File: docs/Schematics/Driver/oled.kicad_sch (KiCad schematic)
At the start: 0 parts

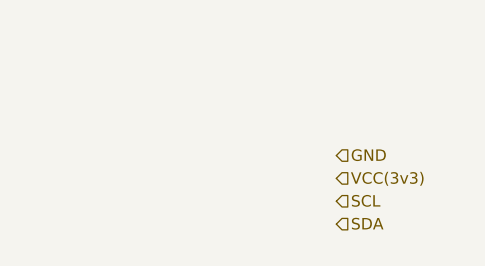
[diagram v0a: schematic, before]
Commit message: First scematic design for the card
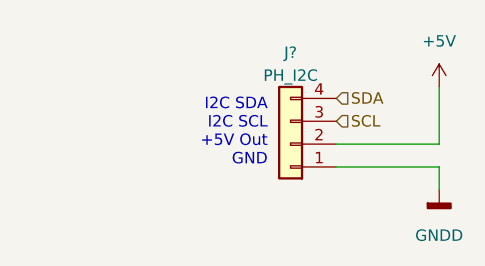
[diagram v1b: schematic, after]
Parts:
- added J?: PH_I2C, symbol Connector_Generic:Conn_01x04
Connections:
- net SCL: now also J?.3 (Pin_3)
- net SDA: now also J?.4 (Pin_4)
- new net +5V: J?.2 (Pin_2)
- new net GNDD: J?.1 (Pin_1)
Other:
- note added: "I2C SDA I2C SCL +5V Out GND"
- company: (none) -> HiQ
- title: (none) -> Arty Z7 IO expander card
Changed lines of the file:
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@@
 (kicad_sch (version 20211123) (generator eeschema)
   (paper "A4")
-  (hierarchical_label "SCL" (shape input) (at 172.72 80.01 0)
+  (title_block
+    (title "Arty Z7 IO expander card")
+    (date "2022-12-24")
+    (rev "0.1")
+    (company "HiQ")
+  )
+  (wire (pts (xy 172.72 73.66) (xy 184.15 73.66))
+    (stroke (width 0) (type default) (color 0 0 0 0))
+  )
+  (wire (pts (xy 172.72 76.2) (xy 184.15 76.2))
+    (stroke (width 0) (type default) (color 0 0 0 0))
+  )
+  (wire (pts (xy 184.15 76.2) (xy 184.15 78.74))
+    (stroke (width 0) (type default) (color 0 0 0 0))
+  )
+  (wire (pts (xy 184.15 73.66) (xy 184.15 67.31))
+    (stroke (width 0) (type default) (color 0 0 0 0))
+  )
+  (text "I2C SDA\nI2C SCL\n+5V Out\nGND" (at 165.1 76.2 180)
+    (effects (font (size 1.27 1.27)) (justify right bottom))
+  )
+  (hierarchical_label "SCL" (shape input) (at 172.72 71.12 0)
     (effects (font (size 1.27 1.27)) (justify left))
   )
-  (hierarchical_label "VCC(3v3)" (shape input) (at 172.72 77.47 0)
+  (hierarchical_label "SDA" (shape input) (at 172.72 68.58 0)
     (effects (font (size 1.27 1.27)) (justify left))
   )
-  (hierarchical_label "GND" (shape input) (at 172.72 74.93 0)
-    (effects (font (size 1.27 1.27)) (justify left))
+  (symbol (lib_id "power:GNDD") (at 184.15 78.74 0) (unit 1)
+    (in_bom yes) (on_board yes) (fields_autoplaced)
+    (property "Reference" "#PWR?" (id 0) (at 184.15 85.09 0)
+      (effects (font (size 1.27 1.27)) hide)
+    )
+    (property "Value" "GNDD" (id 1) (at 184.15 83.82 0))
+    (property "Footprint" "" (id 2) (at 184.15 78.74 0)
+      (effects (font (size 1.27 1.27)) hide)
+    )
+    (property "Datasheet" "" (id 3) (at 184.15 78.74 0)
+      (effects (font (size 1.27 1.27)) hide)
+    )
+    (pin "1")
   )
-  (hierarchical_label "SDA" (shape input) (at 172.72 82.55 0)
-    (effects (font (size 1.27 1.27)) (justify left))
+  (symbol (lib_id "power:+5V") (at 184.15 67.31 0) (unit 1)
+    (in_bom yes) (on_board yes) (fields_autoplaced)
+    (property "Reference" "#PWR?" (id 0) (at 184.15 71.12 0)
+      (effects (font (size 1.27 1.27)) hide)
+    )
+    (property "Value" "+5V" (id 1) (at 184.15 62.23 0))
+    (property "Footprint" "" (id 2) (at 184.15 67.31 0)
+      (effects (font (size 1.27 1.27)) hide)
+    )
+    (property "Datasheet" "" (id 3) (at 184.15 67.31 0)
+      (effects (font (size 1.27 1.27)) hide)
+    )
+    (pin "1")
+  )
+  (symbol (lib_id "Connector_Generic:Conn_01x04") (at 167.64 73.66 180) (unit 1)
+    (in_bom yes) (on_board yes)
+    (property "Reference" "J?" (id 0) (at 167.64 63.5 0))
+    (property "Value" "PH_I2C" (id 1) (at 167.64 66.04 0))
+    (property "Footprint" "" (id 2) (at 167.64 73.66 0)
+      (effects (font (size 1.27 1.27)) hide)
+    )
+    (property "Datasheet" "~" (id 3) (at 167.64 73.66 0)
+      (effects (font (size 1.27 1.27)) hide)
+    )
+    (pin "1")
+    (pin "2")
+    (pin "3")
+    (pin "4")
   )
 )

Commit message: Added footprints and a symbol for the level shifters
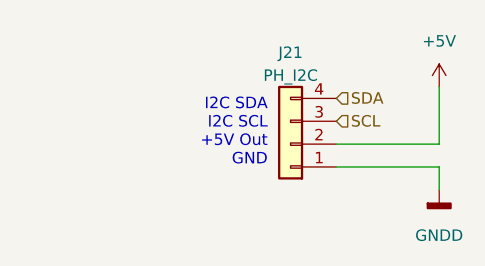
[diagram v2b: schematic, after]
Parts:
- J21: renamed from J?; footprint (none) -> Connector_PinHeader_2.54mm:PinHeader_1x04_P2.54mm_Vertical
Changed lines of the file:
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@@
   (symbol (lib_id "power:GNDD") (at 184.15 78.74 0) (unit 1)
     (in_bom yes) (on_board yes) (fields_autoplaced)
-    (property "Reference" "#PWR?" (id 0) (at 184.15 85.09 0)
+    (property "Reference" "#PWR051" (id 0) (at 184.15 85.09 0)
       (effects (font (size 1.27 1.27)) hide)
     )
@@
   (symbol (lib_id "power:+5V") (at 184.15 67.31 0) (unit 1)
     (in_bom yes) (on_board yes) (fields_autoplaced)
-    (property "Reference" "#PWR?" (id 0) (at 184.15 71.12 0)
+    (property "Reference" "#PWR050" (id 0) (at 184.15 71.12 0)
       (effects (font (size 1.27 1.27)) hide)
     )
@@
   (symbol (lib_id "Connector_Generic:Conn_01x04") (at 167.64 73.66 180) (unit 1)
     (in_bom yes) (on_board yes)
-    (property "Reference" "J?" (id 0) (at 167.64 63.5 0))
+    (property "Reference" "J21" (id 0) (at 167.64 63.5 0))
     (property "Value" "PH_I2C" (id 1) (at 167.64 66.04 0))
-    (property "Footprint" "" (id 2) (at 167.64 73.66 0)
+    (property "Footprint" "Connector_PinHeader_2.54mm:PinHeader_1x04_P2.54mm_Vertical" (id 2) (at 167.64 73.66 0)
       (effects (font (size 1.27 1.27)) hide)
     )

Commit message: Added caps and changed the connection from the motor sensors to plints
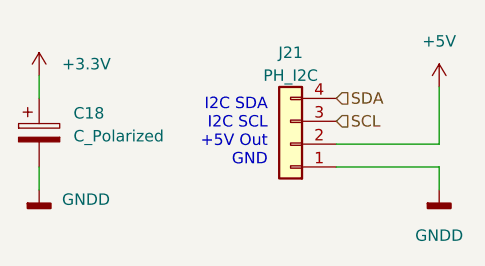
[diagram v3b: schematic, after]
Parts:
- added C18: C_Polarized, Capacitor_THT:CP_Radial_D8.0mm_P3.80mm, symbol Device:C_Polarized
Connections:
- net GNDD: now also C18.2
- new net +3.3V: C18.1
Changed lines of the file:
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@@
+    (stroke (width 0) (type default) (color 0 0 0 0))
+  )
+  (wire (pts (xy 139.7 66.04) (xy 139.7 68.58))
     (stroke (width 0) (type default) (color 0 0 0 0))
   )
   (wire (pts (xy 184.15 76.2) (xy 184.15 78.74))
+    (stroke (width 0) (type default) (color 0 0 0 0))
+  )
+  (wire (pts (xy 139.7 76.2) (xy 139.7 78.74))
     (stroke (width 0) (type default) (color 0 0 0 0))
   )
@@
   (hierarchical_label "SDA" (shape input) (at 172.72 68.58 0)
     (effects (font (size 1.27 1.27)) (justify left))
+  )
+  (symbol (lib_id "power:GNDD") (at 139.7 78.74 0) (unit 1)
+    (in_bom yes) (on_board yes) (fields_autoplaced)
+    (property "Reference" "#PWR096" (id 0) (at 139.7 85.09 0)
+      (effects (font (size 1.27 1.27)) hide)
+    )
+    (property "Value" "GNDD" (id 1) (at 142.24 79.8194 0)
+      (effects (font (size 1.27 1.27)) (justify left))
+    )
+    (property "Footprint" "" (id 2) (at 139.7 78.74 0)
+      (effects (font (size 1.27 1.27)) hide)
+    )
+    (property "Datasheet" "" (id 3) (at 139.7 78.74 0)
+      (effects (font (size 1.27 1.27)) hide)
+    )
+    (pin "1")
+  )
+  (symbol (lib_id "power:+3.3V") (at 139.7 66.04 0) (unit 1)
+    (in_bom yes) (on_board yes) (fields_autoplaced)
+    (property "Reference" "#PWR095" (id 0) (at 139.7 69.85 0)
+      (effects (font (size 1.27 1.27)) hide)
+    )
+    (property "Value" "+3.3V" (id 1) (at 142.24 64.7699 0)
+      (effects (font (size 1.27 1.27)) (justify left))
+    )
+    (property "Footprint" "" (id 2) (at 139.7 66.04 0)
+      (effects (font (size 1.27 1.27)) hide)
+    )
+    (property "Datasheet" "" (id 3) (at 139.7 66.04 0)
+      (effects (font (size 1.27 1.27)) hide)
+    )
+    (pin "1")
   )
   (symbol (lib_id "power:GNDD") (at 184.15 78.74 0) (unit 1)
@@
     (pin "1")
   )
+  (symbol (lib_id "Device:C_Polarized") (at 139.7 72.39 0) (unit 1)
+    (in_bom yes) (on_board yes) (fields_autoplaced)
+    (property "Reference" "C18" (id 0) (at 143.51 70.2309 0)
+      (effects (font (size 1.27 1.27)) (justify left))
+    )
+    (property "Value" "C_Polarized" (id 1) (at 143.51 72.7709 0)
+      (effects (font (size 1.27 1.27)) (justify left))
+    )
+    (property "Footprint" "Capacitor_THT:CP_Radial_D8.0mm_P3.80mm" (id 2) (at 140.6652 76.2 0)
+      (effects (font (size 1.27 1.27)) hide)
+    )
+    (property "Datasheet" "~" (id 3) (at 139.7 72.39 0)
+      (effects (font (size 1.27 1.27)) hide)
+    )
+    (pin "1")
+    (pin "2")
+  )
   (symbol (lib_id "power:+5V") (at 184.15 67.31 0) (unit 1)

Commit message: Started routing the pcb.
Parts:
- C18: footprint Capacitor_THT:CP_Radial_D8.0mm_P3.80mm -> Capacitor_SMD:C_0805_2012Metric_Pad1.18x1.45mm_HandSolder
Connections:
- net +3.3V is gone; now on net +5V: C18.1
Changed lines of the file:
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@@
-    (pin "1")
-  )
-  (symbol (lib_id "power:+3.3V") (at 139.7 66.04 0) (unit 1)
-    (in_bom yes) (on_board yes) (fields_autoplaced)
-    (property "Reference" "#PWR095" (id 0) (at 139.7 69.85 0)
-      (effects (font (size 1.27 1.27)) hide)
-    )
-    (property "Value" "+3.3V" (id 1) (at 142.24 64.7699 0)
-      (effects (font (size 1.27 1.27)) (justify left))
-    )
-    (property "Footprint" "" (id 2) (at 139.7 66.04 0)
-      (effects (font (size 1.27 1.27)) hide)
-    )
-    (property "Datasheet" "" (id 3) (at 139.7 66.04 0)
-      (effects (font (size 1.27 1.27)) hide)
-    )
     (pin "1")
   )
@@
       (effects (font (size 1.27 1.27)) (justify left))
     )
-    (property "Footprint" "Capacitor_THT:CP_Radial_D8.0mm_P3.80mm" (id 2) (at 140.6652 76.2 0)
+    (property "Footprint" "Capacitor_SMD:C_0805_2012Metric_Pad1.18x1.45mm_HandSolder" (id 2) (at 140.6652 76.2 0)
       (effects (font (size 1.27 1.27)) hide)
     )
@@
     (pin "2")
   )
+  (symbol (lib_id "power:+5V") (at 139.7 66.04 0) (unit 1)
+    (in_bom yes) (on_board yes) (fields_autoplaced)
+    (property "Reference" "#PWR0101" (id 0) (at 139.7 69.85 0)
+      (effects (font (size 1.27 1.27)) hide)
+    )
+    (property "Value" "+5V" (id 1) (at 139.7 60.96 0))
+    (property "Footprint" "" (id 2) (at 139.7 66.04 0)
+      (effects (font (size 1.27 1.27)) hide)
+    )
+    (property "Datasheet" "" (id 3) (at 139.7 66.04 0)
+      (effects (font (size 1.27 1.27)) hide)
+    )
+    (pin "1")
+  )
   (symbol (lib_id "power:+5V") (at 184.15 67.31 0) (unit 1)

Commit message: First version of the routed board is done
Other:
- title: Arty Z7 IO expander card -> Arty Z7 IO Board
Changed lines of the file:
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@@
   (paper "A4")
   (title_block
-    (title "Arty Z7 IO expander card")
+    (title "Arty Z7 IO Board")
     (date "2022-12-24")
-    (rev "0.1")
+    (rev "${VER}")
     (company "HiQ")
   )
